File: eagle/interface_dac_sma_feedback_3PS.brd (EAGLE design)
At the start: 128.5 x 101.9 mm, 14 parts

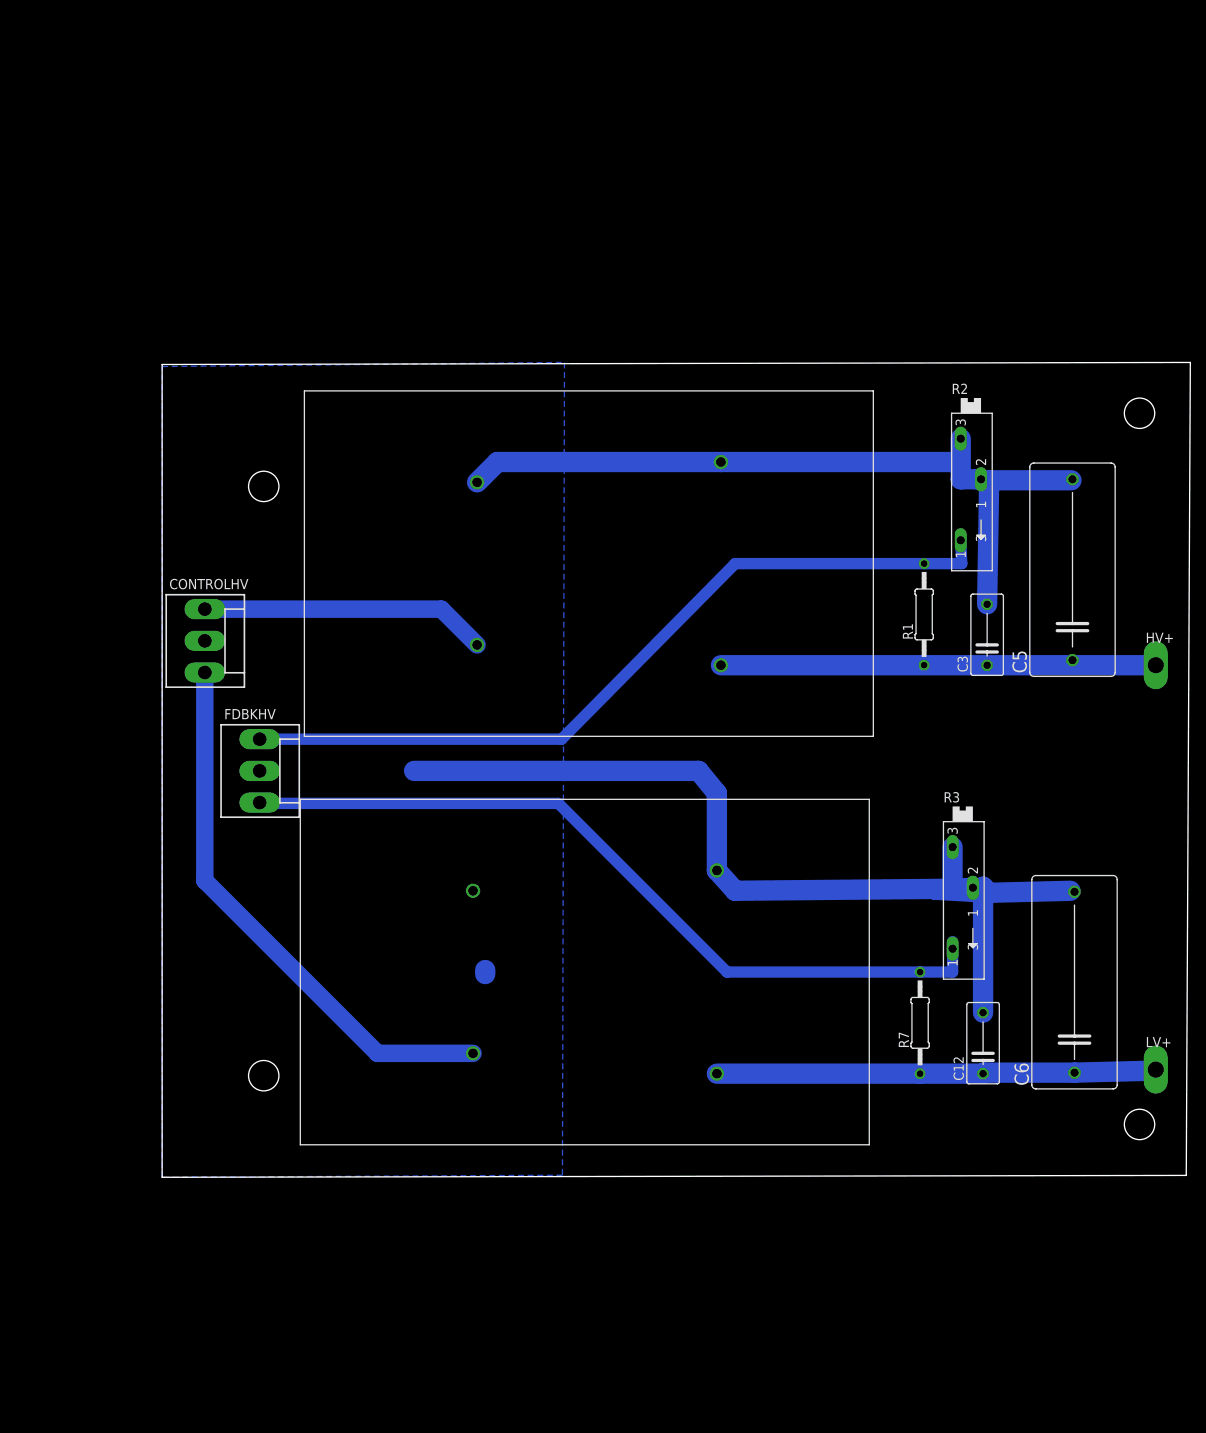
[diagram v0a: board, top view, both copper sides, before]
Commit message: 3PS, 2 1kV in parallel
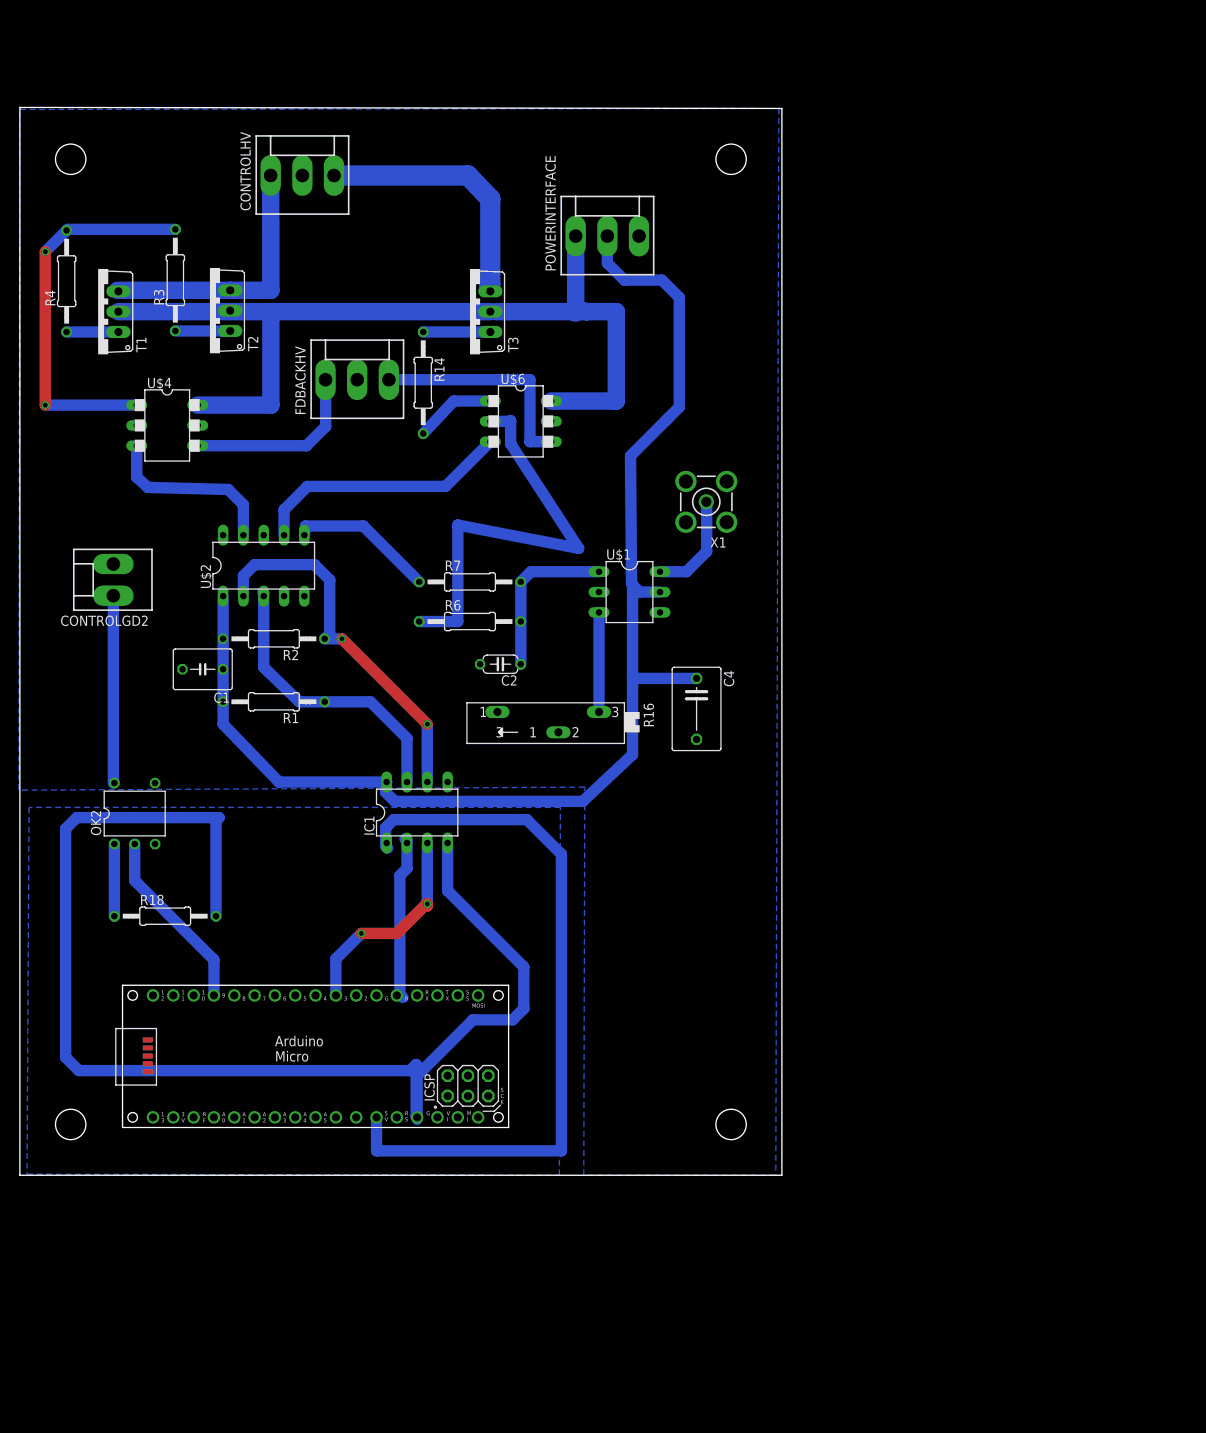
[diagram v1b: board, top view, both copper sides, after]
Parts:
- removed C12, C3: .01u, rcl:C075-042X103
- removed C5, C6: 1u, rcl:C225-108X268
- removed FDBKHV: (no value), con-molex:KK-156-3
- removed HV+, LV+: TPPAD1-20Y, testpad:P1-20Y
- added C1: (no value), rcl:C050-050X075
- added C2: 10n, resistor:C050-024X044
- added C4: (no value), resistor:C075-063X106
- added CONTROLGD2: (no value), con-molex:KK-156-2
- added FDBACKHV, POWERINTERFACE: (no value), con-molex:KK-156-3
- added IC1: ISO1540, texas:DIL08
- added OK2: H11F1, optocoupler:DIL05
- added PCB1: ARDUINO_MICRO, E14_Arduino_published:ARDUINO_MICRO
- added R14, R4: 1k, resistor:0207/12
- added R16: (no value), pot:SP19L
- added R18: 100, rcl:0207/12
- added R6: 10k, resistor:0207/12
- added T1, T2, T3: TIP122V, transistor-npn:TO220V
- added U$4, U$6: MAX9650DIL, maxim:DIL06-4
- added X1: BU-SMA-V, con-coax:BU-SMA-V
- R1: value 2M -> 1.5k
- R2: value (none) -> 1.5k; device pot:SP19L -> resistor:0207/12
- R3: value (none) -> 1k; device pot:SP19L -> resistor:0207/12
- R7: value 2M -> 40k
- U$1: value EMCO-F104PIN -> LTC6992; device dc-dc-converter:EMCO-F -> linear-technology:DIL06
- U$2: value EMCO-F104PIN -> MCP4728DIL; device dc-dc-converter:EMCO-F -> microchip:DIL10
- moved R3 125.5 mm to (19.4, 111.9), turned to 90 degrees
- moved R2 89.0 mm to (31.8, 67.1), turned to 180 degrees
- moved R1 82.0 mm to (31.8, 59.2), turned to 180 degrees
- moved R7 78.8 mm to (56.3, 74.2), turned to 0 degrees
- moved U$2 66.3 mm to (30.5, 76.2)
- moved CONTROLHV 59.4 mm to (35.3, 125.0), turned to 0 degrees
- moved U$1 20.2 mm to (76.2, 72.9), turned to 270 degrees
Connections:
- new net +12V: POWERINTERFACE.1, T1.2, T2.2, T3.2, U$4.6, U$6.6
- new net A+5: IC1.1, PCB1.+5V
- new net AGND: IC1.4, PCB1.GND., R18.2
- new net D10: PCB1.D10
- new net D11: PCB1.D11
- new net D4: PCB1.D4
- new net D7: PCB1.D7
- new net D8: PCB1.D8
- new net ENSW2: CONTROLGD2.1, OK2.6
- new net N$12: R16.E, U$1.SET
- new net N$13: U$1.OUT, X1.1
- new net N$14: FDBACKHV.3, U$6.4
- new net N$15: R14.1, T3.1
- new net N$16: U$2.9, U$4.3
- new net N$17: U$2.8
- new net N$18: U$2.7, U$6.3
- new net N$19: R3.2, R4.2, U$4.1
- new net N$21: R14.2, U$6.1
- new net N$6: R3.1, T2.1
- new net N$7: OK2.1, R18.1
- new net PWM5: PCB1.D5
- new net PWM6: PCB1.D6
- new net PWM9: OK2.2, PCB1.D9
- new net SCL: IC1.3, PCB1.D3
- new net SCL_OUT: IC1.6, R2.1, U$2.2
- new net SDA: IC1.2, PCB1.D2
- new net SDA_OUT: IC1.7, R1.1, U$2.3
- new net VCC: C1.1, C4.1, IC1.8, POWERINTERFACE.2, R1.2, R2.2, U$1.VCC, U$2.1
- net GND: now also C1.2, C2.2, C4.2, CONTROLGD2.2, FDBACKHV.2, IC1.5, OK2.4, POWERINTERFACE.3, R16.A, R16.S, R6.1, U$1.DIV, U$1.GND, U$2.10, U$2.4, U$4.2, U$6.2, X1.2, X1.3, X1.4, X1.5; no longer C12.2, C3.2, C5.2, C6.2, FDBKHV.2, R2.E, R2.S, R3.E, R3.S, U$1.P$2, U$1.P$4, U$2.P$2, U$2.P$4
- net N$1: now also R7.1, U$2.6; no longer C3.1, C5.1, HV+.TP, R1.1, U$1.P$3
- net N$2: now also C2.1, R6.2, R7.2, U$1.MOD; no longer C12.1, C6.1, LV+.TP, R7.1, U$2.P$3
- net N$3: now also R4.1, T1.1; no longer FDBKHV.1, R1.2, R2.A
- net N$4: now also T1.3, T2.3; no longer U$1.P$1
- net N$5: now also T3.3; no longer U$2.P$1
- net N$8: now also FDBACKHV.1, U$4.4; no longer FDBKHV.3, R3.A, R7.2
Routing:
- net GND: track 222.6 -> 53.3 mm
- net VCC: track 0.00 -> 160.7 mm
- net AGND: track 0.00 -> 159.2 mm
- net +12V: track 0.00 -> 113.6 mm
- net N$3: track 99.8 -> 6.48 mm
- net A+5: track 0.00 -> 91.2 mm
- net N$8: track 99.5 -> 22.8 mm
- net N$19: track 0.00 -> 48.0 mm, vias 0 -> 2
- net SCL_OUT: track 0.00 -> 46.8 mm, vias 0 -> 2
- net N$5: track 68.5 -> 31.8 mm
- net SDA_OUT: track 0.00 -> 36.5 mm
- net N$1: track 54.4 -> 18.3 mm
- net N$2: track 55.0 -> 20.6 mm
- net N$18: track 0.00 -> 32.5 mm
- net N$14: track 0.00 -> 28.0 mm
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- added copper zone on layer 16, net AGND
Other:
- board size 128.5 x 101.9 mm -> 95.2 x 133.5 mm

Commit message: tweaks. still need bigger vias for zeners and hv resistors
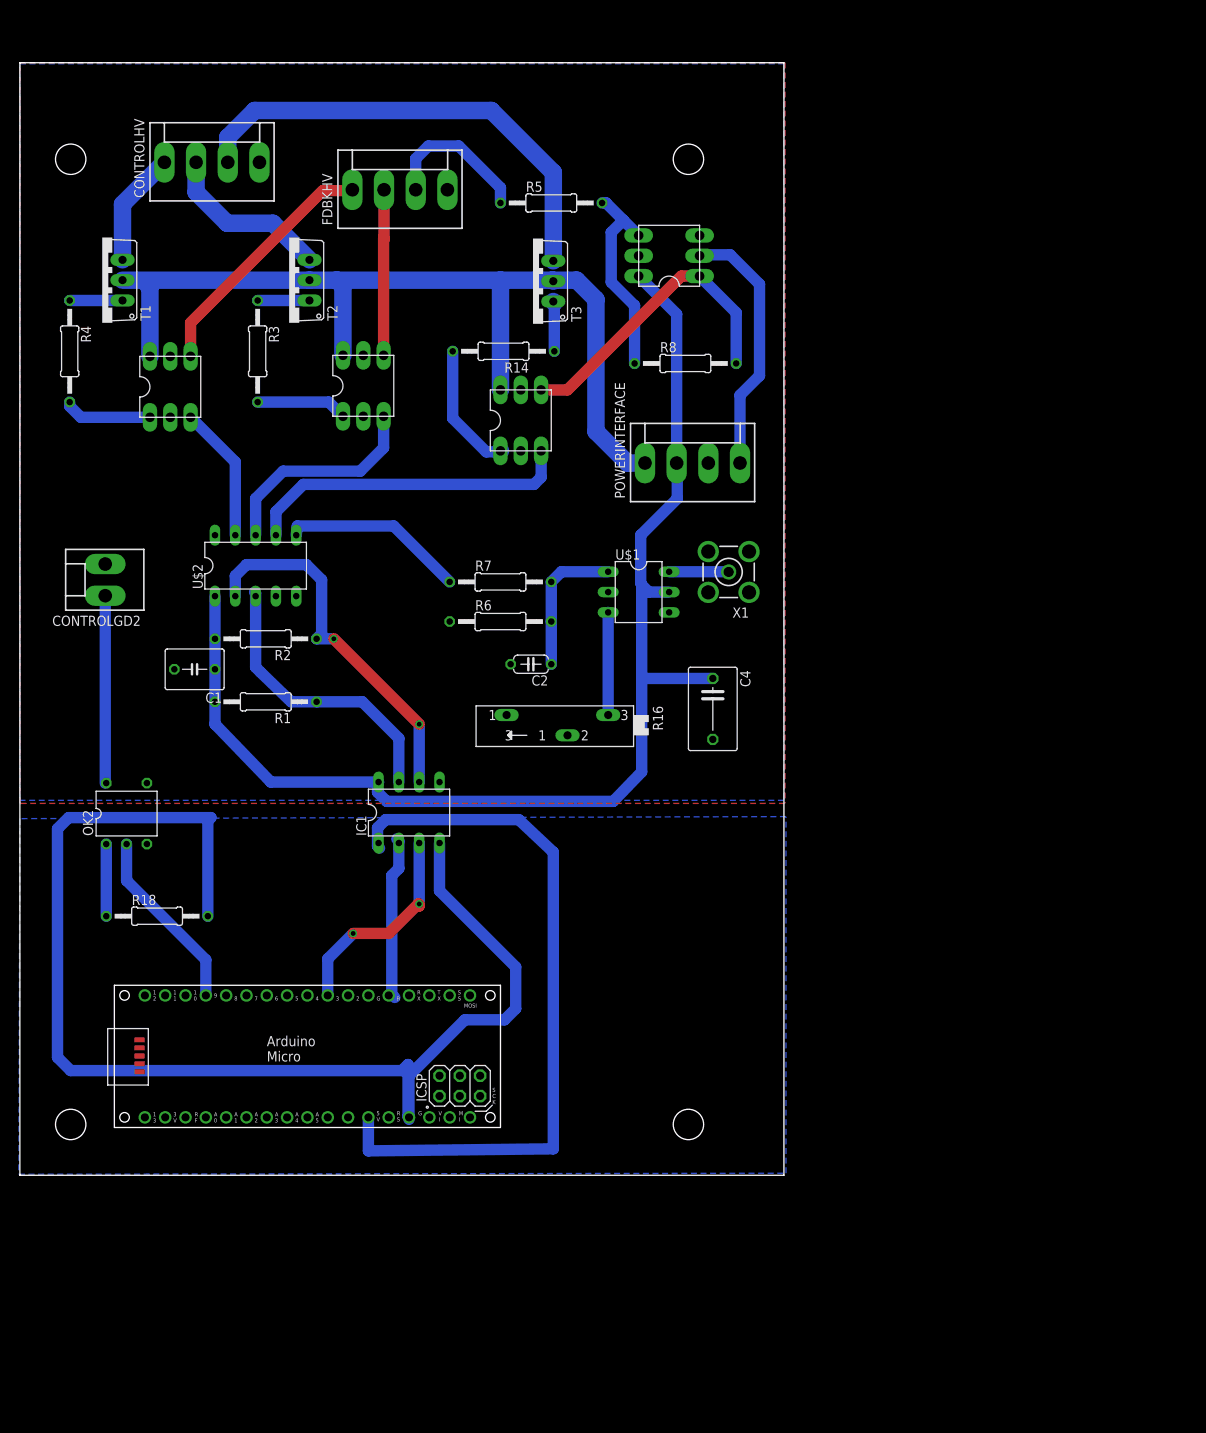
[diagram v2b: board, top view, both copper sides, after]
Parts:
- removed FDBACKHV: (no value), con-molex:KK-156-3
- added FDBKHV: (no value), con-molex:KK-156-4
- added R5, R8: 1k, resistor:0207/12
- added U$3, U$5: OPA735DIL, texas:DIL6
- CONTROLHV, POWERINTERFACE: device con-molex:KK-156-3 -> con-molex:KK-156-4
- U$4, U$6: value MAX9650DIL -> OPA735DIL; device maxim:DIL06-4 -> texas:DIL6
- moved U$4 44.2 mm to (62.6, 94.4), turned to 0 degrees
- moved U$6 44.0 mm to (18.8, 98.6), turned to 0 degrees
- moved POWERINTERFACE 30.3 mm to (84.1, 89.0)
- moved R3 13.6 mm to (29.7, 103.0), turned to 270 degrees
- moved CONTROLHV 11.4 mm to (24.0, 126.6)
- moved R14 10.8 mm to (60.5, 103.0), turned to 180 degrees
- moved T2 10.6 mm to (33.7, 111.9)
- moved X1 9.20 mm to (88.6, 75.4)
- moved R4 8.77 mm to (6.22, 103.0), turned to 270 degrees
- moved T3 8.75 mm to (64.1, 111.8)
- moved T1 3.97 mm to (10.3, 111.9)
- moved C2 3.81 mm to (63.9, 63.9)
- moved R6 3.81 mm to (60.1, 69.2)
- moved R7 3.81 mm to (60.1, 74.2)
- moved C4 2.03 mm to (86.6, 58.3)
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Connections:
- new net -5V: POWERINTERFACE.4, U$3.P$2
- new net N$10: R3.2, U$5.P$1
- new net N$11: CONTROLHV.2, T2.3
- new net N$23: R5.2, R8.1, U$3.P$4
- new net N$6: FDBKHV.2, U$5.P$4
- new net N$9: FDBKHV.3, R5.1
- net +12V: now also U$4.P$6, U$5.P$6, U$6.P$6; no longer U$4.6, U$6.6
- net GND: now also CONTROLHV.4, FDBKHV.4, U$3.P$3, U$4.P$2, U$5.P$2, U$6.P$2; no longer CONTROLHV.2, FDBACKHV.2, U$4.2, U$6.2
- net N$14: now also R8.2, U$3.P$1, U$4.P$4; no longer FDBACKHV.3, U$6.4
- net N$16: now also U$6.P$3; no longer U$4.3
- net N$17: now also U$5.P$3
- net N$18: now also U$4.P$3; no longer U$6.3
- net N$19: now also U$6.P$1; no longer R3.2, U$4.1
- net N$21: now also U$4.P$1; no longer U$6.1
- net N$4: no longer T2.3
- net N$8: now also FDBKHV.1, U$6.P$4; no longer FDBACKHV.1, U$4.4
- net VCC: now also U$3.P$6
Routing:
- net GND: track 53.3 -> 0.00 mm
- net N$19: track 48.0 -> 11.1 mm, vias 2 -> 0
- net -5V: track 0.00 -> 32.4 mm
- net N$5: track 31.8 -> 59.5 mm
- net N$17: track 0.00 -> 27.1 mm
- net N$23: track 0.00 -> 26.0 mm
- net N$11: track 0.00 -> 21.4 mm
- net N$6: track 0.00 -> 21.1 mm
- net N$9: track 0.00 -> 19.2 mm
- net N$4: track 33.5 -> 14.4 mm
- net N$10: track 0.00 -> 11.4 mm
- net N$14: track 28.0 -> 38.5 mm
- net N$18: track 32.5 -> 41.2 mm
- net N$8: track 22.8 -> 31.3 mm
- net VCC: track 160.7 -> 154.5 mm
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- added copper zone on layer 1, net GND
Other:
- board size 95.2 x 133.5 mm -> 95.5 x 139.1 mm
